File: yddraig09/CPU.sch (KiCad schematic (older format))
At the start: 6 parts

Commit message: Added RAM/ROM Banking idea
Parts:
- removed U?: SST39SF020, symbol Memory_Flash:SST39SF020
- removed U?: AT28C64B, symbol Ddraig:AT28C64B
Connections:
- net labels removed: A0, A1, A10, A11, A12, A13, A2, A3, A4, A5, A6, A7, A8, A9, RB0, RB1, RB2, RB3
- wire segments 124 -> 67
- no-connect marks 1 -> 0

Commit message: Some tidying up of 6809 project
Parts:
- added C? (x2): 10uF, Capacitor_THT:CP_Radial_D5.0mm_P2.50mm, symbol Device:CP
- added C?: 10nF, Capacitor_THT:C_Disc_D3.8mm_W2.6mm_P2.50mm, symbol Device:C
- added C? (x2): 22pF, Capacitor_THT:C_Disc_D5.0mm_W2.5mm_P2.50mm, symbol Device:C
- added C?: 5pF, Capacitor_THT:C_Disc_D5.0mm_W2.5mm_P2.50mm, symbol Device:C
- added J?: ExtReset, Connector_PinHeader_2.54mm:PinHeader_1x02_P2.54mm_Vertical, symbol Connector_Generic:Conn_01x02
- added R?: 10K, Resistor_THT:R_Axial_DIN0207_L6.3mm_D2.5mm_P10.16mm_Horizontal, symbol Device:R
- added R?: 38K, Resistor_THT:R_Axial_DIN0207_L6.3mm_D2.5mm_P10.16mm_Horizontal, symbol Device:R
- added R? (x4): 4k7, symbol Device:R
- added R?: 4M7, Resistor_THT:R_Axial_DIN0207_L6.3mm_D2.5mm_P10.16mm_Horizontal, symbol Device:R
- added R?: 2K2, Resistor_THT:R_Axial_DIN0207_L6.3mm_D2.5mm_P10.16mm_Horizontal, symbol Device:R
- added SW?: Reset, Button_Switch_THT:SW_PUSH_6mm_H4.3mm, symbol Switch:SW_SPST
- added U?: NE555P, Package_DIP:DIP-8_W7.62mm, symbol Timer:NE555P
- added U? (x7): 74HCT04, symbol 74xx:74HCT04
- added Y?: 8Mhz, Crystal:Crystal_HC50_Vertical, symbol Device:Crystal
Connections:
- net +5V: now also U?.39 (TSC), R?.1, R?.1, R?.1, R?.1, R?.1, R?.1, U?.14 (VCC), U?.4 (R), U?.8 (VCC)
- net GND: now also C?.2, C?.2, C?.2, C?.2, C?.2, C?.2, J?.2 (Pin_2), SW?.1 (A), U?.1 (GND), U?.11, U?.5, U?.7 (GND), U?.9
- net RD~WR: now also U?.32 (R/~W)
- net CPU_A2: now reaches U?.10 (A2)
- net CPU_A3: now reaches U?.11 (A3)
- net CPU_A4: now reaches U?.12 (A4)
- net CPU_A5: now reaches U?.13 (A5)
- net CPU_A6: now reaches U?.14 (A6)
- net CPU_A7: now reaches U?.15 (A7)
- net CPU_A8: now reaches U?.16 (A8)
- net CPU_A9: now reaches U?.17 (A9)
- net CPU_A10: now reaches U?.18 (A10)
- net CPU_A11: now reaches U?.19 (A11)
- net at U?.2 (~NMI): now also R?.2
- net CPU_A12: now reaches U?.20 (A12)
- net CPU_A13: now reaches U?.21 (A13)
- net CPU_A14: now reaches U?.22 (A14)
- net CPU_A15: now reaches U?.23 (A15)
- net at U?.3 (~IRQ): now also R?.2
- net ~RESET: now reaches U?.37 (~RESET)
- net ~RESET: now also U?.12
- net at U?.4 (~FIRQ): now also R?.2
- net ~HALT: now reaches U?.40 (~HALT)
- net ~HALT: now also R?.2
- net BS: now reaches U?.5 (BS)
- net BA: now reaches U?.6 (BA)
- net CPU_A0: now reaches U?.8 (A0)
- net CPU_A1: now reaches U?.9 (A1)
- net CLK8M renamed CLK_8MHZ
- net CLK_8MHZ: now also C?.1, R?.1
- net D0 renamed CPU_D0
- net D1 renamed CPU_D1
- net D2 renamed CPU_D2
- net D3 renamed CPU_D3
- net D4 renamed CPU_D4
- net D5 renamed CPU_D5
- net D6 renamed CPU_D6
- net D7 renamed CPU_D7
- new net: C?.1, J?.1 (Pin_1), R?.2, SW?.2 (B), U?.2 (TR)
- new net: C?.1, U?.5 (CV)
- new net: C?.1, R?.2, U?.6 (THR), U?.7 (DIS)
- new net: C?.1, R?.1, U?.1, Y?.2
- new net: C?.1, R?.2, U?.2, U?.3, Y?.1
- new net: R?.2, U?.4
- new net RESET: U?.13, U?.3 (Q)
- no-connect marks 0 -> 6
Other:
- moved on the sheet: U?, U?A, U?B, U?C

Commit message: more progress
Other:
- moved on the sheet: C?, R?, U?A, U?B, Y?

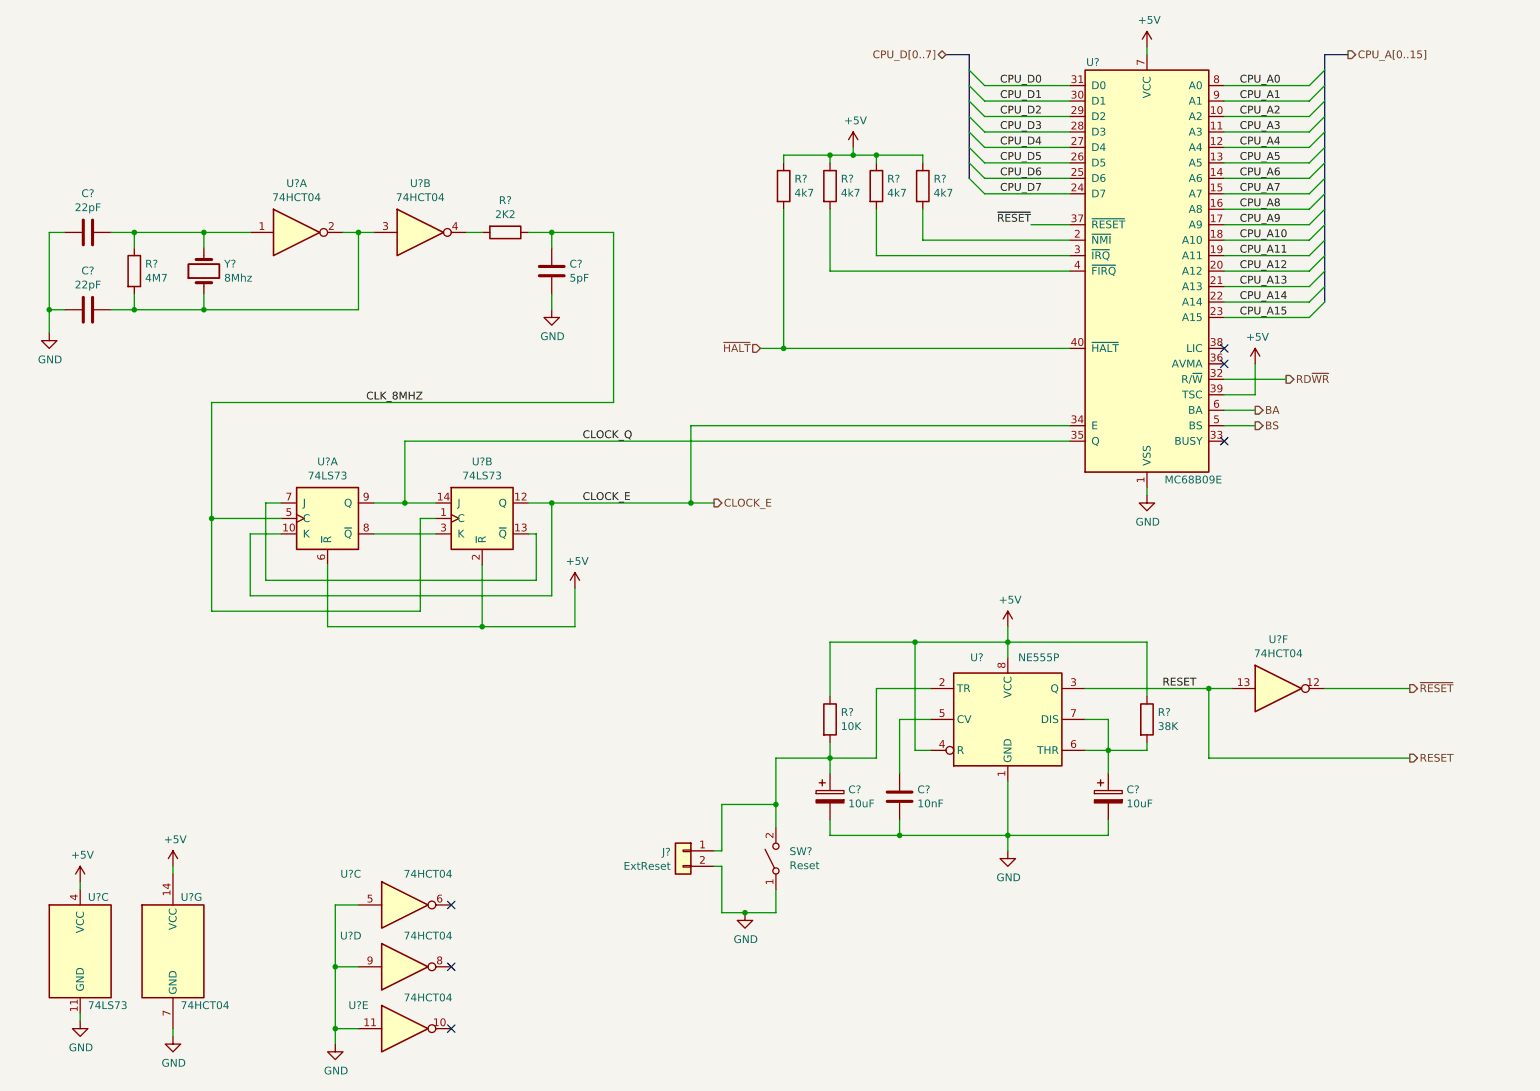
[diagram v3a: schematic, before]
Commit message: ddraig09: Added decode logic and expansion slot
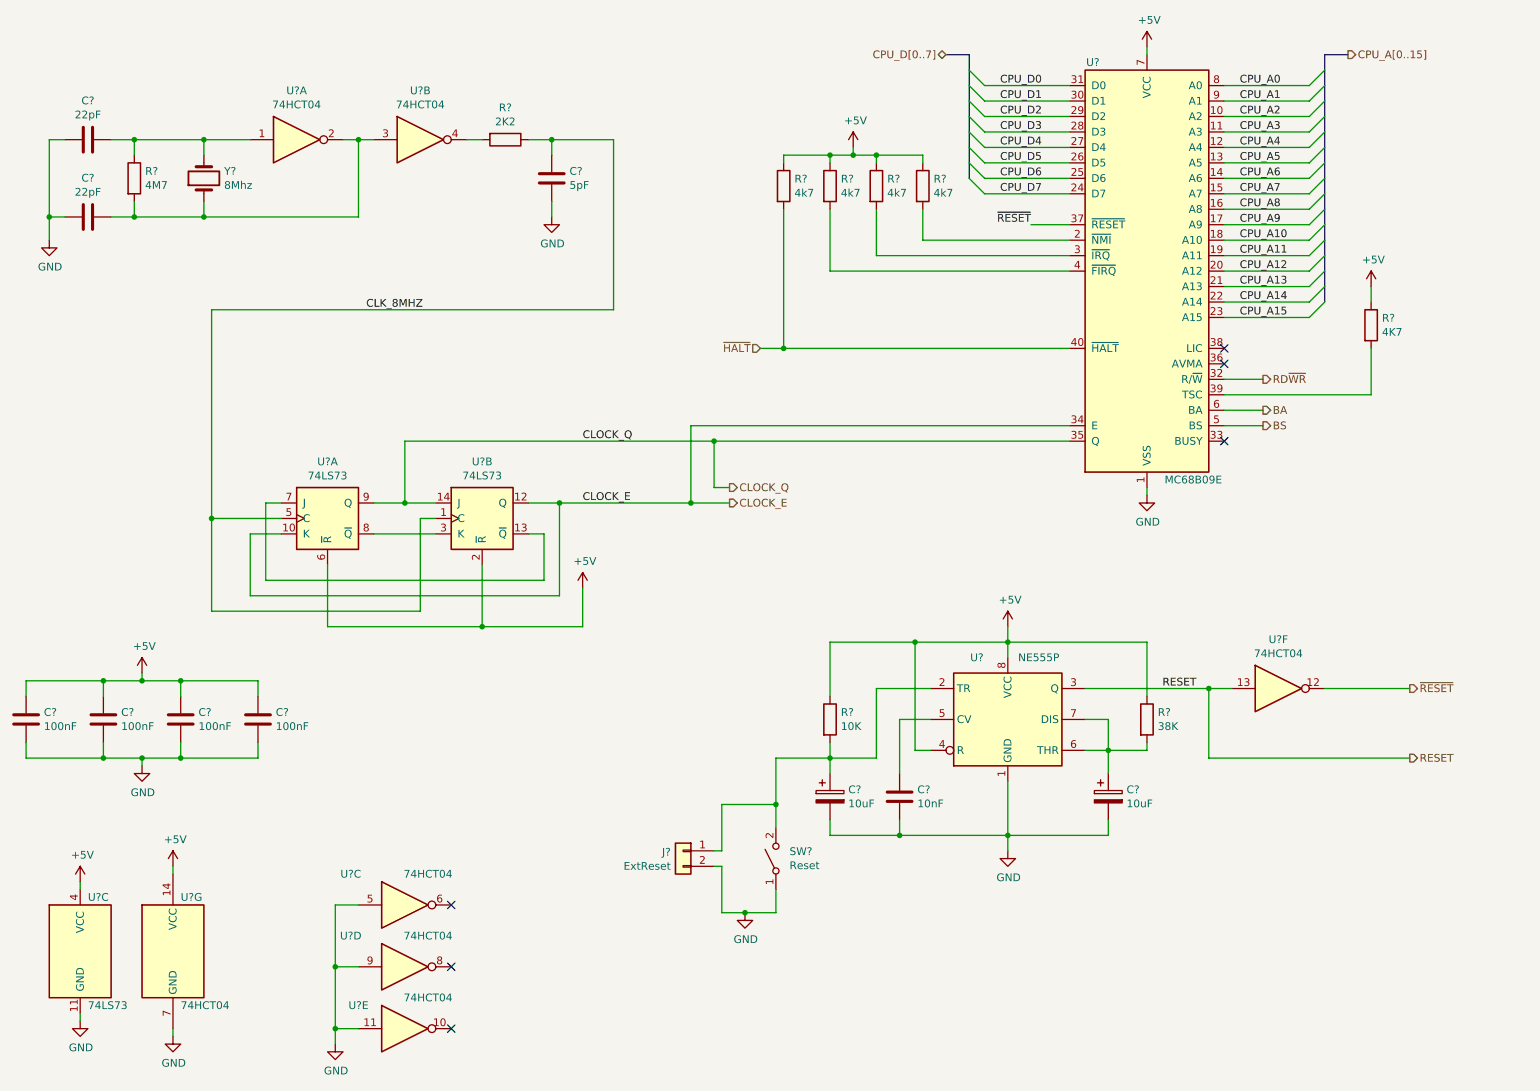
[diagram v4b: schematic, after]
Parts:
- added C? (x4): 100nF, symbol Device:C
- added R?: 4K7, symbol Device:R
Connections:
- net +5V: now also C?.1, C?.1, C?.1, C?.1, R?.1; no longer U?.39 (TSC)
- net GND: now also C?.2, C?.2, C?.2, C?.2
- new net: R?.2, U?.39 (TSC)
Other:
- moved on the sheet: C?, R?, U?A, U?B, Y?

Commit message: ddraig09: initial design done
Need to be reviewed and decode on additional uses for IO but passed DRC
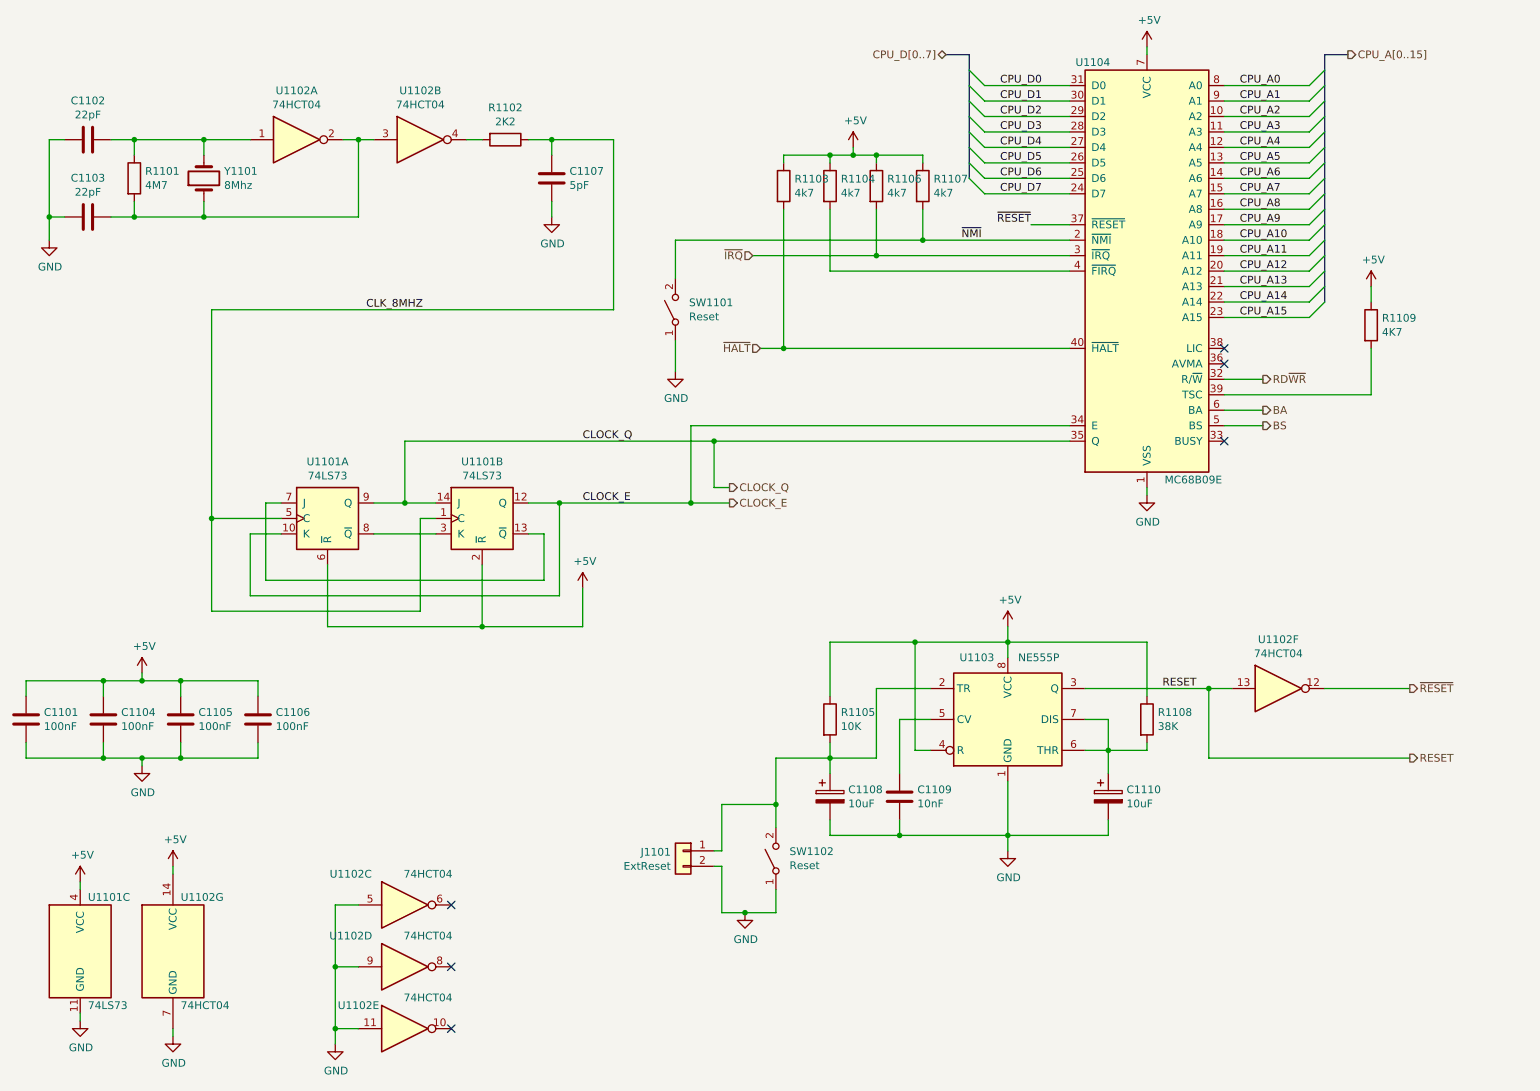
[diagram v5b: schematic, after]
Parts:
- added SW1101: Reset, Button_Switch_THT:SW_PUSH_6mm_H4.3mm, symbol Switch:SW_SPST
- gave numbers to parts that had none: 26
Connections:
- net GND: now also SW1101.1 (A)
- net ~NMI: now reaches R1107.2, U1104.2 (~NMI)
- net ~NMI: now also SW1101.2 (B)
- net ~IRQ: now reaches R1106.2, U1104.3 (~IRQ)

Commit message: Asssigned part footprints to most of schematic
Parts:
- C1101, C1104, C1105, C1106: footprint (none) -> Capacitor_THT:C_Disc_D5.0mm_W2.5mm_P2.50mm
- R1103, R1104, R1106, R1107, R1109: footprint (none) -> Resistor_THT:R_Axial_DIN0207_L6.3mm_D2.5mm_P10.16mm_Horizontal
- U1101, U1102: footprint (none) -> Package_DIP:DIP-14_W7.62mm_Socket
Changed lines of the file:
@@
 F 0 "U1101" H 1750 7200 50  0000 L CNN
 F 1 "74LS73" H 1750 6500 50  0000 L CNN
-F 2 "" H 1700 6850 50  0001 C CNN
+F 2 "Package_DIP:DIP-14_W7.62mm_Socket" H 1700 6850 50  0001 C CNN
 F 3 "http://www.ti.com/lit/gpn/sn74LS73" H 1700 6850 50  0001 C CNN
 	3    1700 6850
@@
 F 0 "R1106" H 6920 1946 50  0000 L CNN
 F 1 "4k7" H 6920 1855 50  0000 L CNN
-F 2 "" V 6780 1900 50  0001 C CNN
+F 2 "Resistor_THT:R_Axial_DIN0207_L6.3mm_D2.5mm_P10.16mm_Horizontal" V 6780 1900 50  0001 C CNN
 F 3 "~" H 6850 1900 50  0001 C CNN
 	1    6850 1900
@@
 F 0 "R1107" H 7220 1946 50  0000 L CNN
 F 1 "4k7" H 7220 1855 50  0000 L CNN
-F 2 "" V 7080 1900 50  0001 C CNN
+F 2 "Resistor_THT:R_Axial_DIN0207_L6.3mm_D2.5mm_P10.16mm_Horizontal" V 7080 1900 50  0001 C CNN
 F 3 "~" H 7150 1900 50  0001 C CNN
 	1    7150 1900
@@
 F 0 "R1103" H 6320 1946 50  0000 L CNN
 F 1 "4k7" H 6320 1855 50  0000 L CNN
-F 2 "" V 6180 1900 50  0001 C CNN
+F 2 "Resistor_THT:R_Axial_DIN0207_L6.3mm_D2.5mm_P10.16mm_Horizontal" V 6180 1900 50  0001 C CNN
 F 3 "~" H 6250 1900 50  0001 C CNN
 	1    6250 1900
@@
 F 0 "R1104" H 6620 1946 50  0000 L CNN
 F 1 "4k7" H 6620 1855 50  0000 L CNN
-F 2 "" V 6480 1900 50  0001 C CNN
+F 2 "Resistor_THT:R_Axial_DIN0207_L6.3mm_D2.5mm_P10.16mm_Horizontal" V 6480 1900 50  0001 C CNN
 F 3 "~" H 6550 1900 50  0001 C CNN
 	1    6550 1900
@@
 F 0 "U1102" H 3450 6750 50  0000 C CNN
 F 1 "74HCT04" H 3950 6750 50  0000 C CNN
-F 2 "" H 3800 6550 50  0001 C CNN
+F 2 "Package_DIP:DIP-14_W7.62mm_Socket" H 3800 6550 50  0001 C CNN
 F 3 "https://assets.nexperia.com/documents/data-sheet/74HC_HCT04.pdf" H 3800 6550 50  0001 C CNN
 	3    3800 6550
@@
 F 0 "U1102" H 3450 7150 50  0000 C CNN
 F 1 "74HCT04" H 3950 7150 50  0000 C CNN
-F 2 "" H 3800 6950 50  0001 C CNN
+F 2 "Package_DIP:DIP-14_W7.62mm_Socket" H 3800 6950 50  0001 C CNN
 F 3 "https://assets.nexperia.com/documents/data-sheet/74HC_HCT04.pdf" H 3800 6950 50  0001 C CNN
 	4    3800 6950
@@
 F 0 "U1102" H 3500 7500 50  0000 C CNN
 F 1 "74HCT04" H 3950 7550 50  0000 C CNN
-F 2 "" H 3800 7350 50  0001 C CNN
+F 2 "Package_DIP:DIP-14_W7.62mm_Socket" H 3800 7350 50  0001 C CNN
 F 3 "https://assets.nexperia.com/documents/data-sheet/74HC_HCT04.pdf" H 3800 7350 50  0001 C CNN
 	5    3800 7350
@@
 F 0 "U1102" H 9450 5467 50  0000 C CNN
 F 1 "74HCT04" H 9450 5376 50  0000 C CNN
-F 2 "" H 9450 5150 50  0001 C CNN
+F 2 "Package_DIP:DIP-14_W7.62mm_Socket" H 9450 5150 50  0001 C CNN
 F 3 "https://assets.nexperia.com/documents/data-sheet/74HC_HCT04.pdf" H 9450 5150 50  0001 C CNN
 	6    9450 5150
@@
 F 0 "U1102" H 2350 7200 50  0000 L CNN
 F 1 "74HCT04" H 2350 6500 50  0000 L CNN
-F 2 "" H 2300 6850 50  0001 C CNN
+F 2 "Package_DIP:DIP-14_W7.62mm_Socket" H 2300 6850 50  0001 C CNN
 F 3 "https://assets.nexperia.com/documents/data-sheet/74HC_HCT04.pdf" H 2300 6850 50  0001 C CNN
 	7    2300 6850
@@
 F 0 "U1102" H 3900 1917 50  0000 C CNN
 F 1 "74HCT04" H 3900 1826 50  0000 C CNN
-F 2 "" H 3900 1600 50  0001 C CNN
+F 2 "Package_DIP:DIP-14_W7.62mm_Socket" H 3900 1600 50  0001 C CNN
 F 3 "https://assets.nexperia.com/documents/data-sheet/74HC_HCT04.pdf" H 3900 1600 50  0001 C CNN
 	2    3900 1600
@@
 F 0 "U1102" H 3100 1917 50  0000 C CNN
 F 1 "74HCT04" H 3100 1826 50  0000 C CNN
-F 2 "" H 3100 1600 50  0001 C CNN
+F 2 "Package_DIP:DIP-14_W7.62mm_Socket" H 3100 1600 50  0001 C CNN
 F 3 "https://assets.nexperia.com/documents/data-sheet/74HC_HCT04.pdf" H 3100 1600 50  0001 C CNN
 	1    3100 1600
@@
 F 0 "U1101" H 3300 4417 50  0000 C CNN
 F 1 "74LS73" H 3300 4326 50  0000 C CNN
-F 2 "" H 3300 4050 50  0001 C CNN
+F 2 "Package_DIP:DIP-14_W7.62mm_Socket" H 3300 4050 50  0001 C CNN
 F 3 "http://www.ti.com/lit/gpn/sn74LS73" H 3300 4050 50  0001 C CNN
 	1    3300 4050
@@
 F 0 "U1101" H 4300 4417 50  0000 C CNN
 F 1 "74LS73" H 4300 4326 50  0000 C CNN
-F 2 "" H 4300 4050 50  0001 C CNN
+F 2 "Package_DIP:DIP-14_W7.62mm_Socket" H 4300 4050 50  0001 C CNN
 F 3 "http://www.ti.com/lit/gpn/sn74LS73" H 4300 4050 50  0001 C CNN
 	2    4300 4050
@@
 F 0 "R1109" H 10120 2846 50  0000 L CNN
 F 1 "4K7" H 10120 2755 50  0000 L CNN
-F 2 "" V 9980 2800 50  0001 C CNN
+F 2 "Resistor_THT:R_Axial_DIN0207_L6.3mm_D2.5mm_P10.16mm_Horizontal" V 9980 2800 50  0001 C CNN
 F 3 "~" H 10050 2800 50  0001 C CNN
 	1    10050 2800
@@
 F 0 "C1101" H 1465 5396 50  0000 L CNN
 F 1 "100nF" H 1465 5305 50  0000 L CNN
-F 2 "" H 1388 5200 50  0001 C CNN
+F 2 "Capacitor_THT:C_Disc_D5.0mm_W2.5mm_P2.50mm" H 1388 5200 50  0001 C CNN
 F 3 "~" H 1350 5350 50  0001 C CNN
 	1    1350 5350
@@
 F 0 "C1104" H 1965 5396 50  0000 L CNN
 F 1 "100nF" H 1965 5305 50  0000 L CNN
-F 2 "" H 1888 5200 50  0001 C CNN
+F 2 "Capacitor_THT:C_Disc_D5.0mm_W2.5mm_P2.50mm" H 1888 5200 50  0001 C CNN
 F 3 "~" H 1850 5350 50  0001 C CNN
 	1    1850 5350
@@
 F 0 "C1105" H 2465 5396 50  0000 L CNN
 F 1 "100nF" H 2465 5305 50  0000 L CNN
-F 2 "" H 2388 5200 50  0001 C CNN
+F 2 "Capacitor_THT:C_Disc_D5.0mm_W2.5mm_P2.50mm" H 2388 5200 50  0001 C CNN
 F 3 "~" H 2350 5350 50  0001 C CNN
 	1    2350 5350
@@
 F 0 "C1106" H 2965 5396 50  0000 L CNN
 F 1 "100nF" H 2965 5305 50  0000 L CNN
-F 2 "" H 2888 5200 50  0001 C CNN
+F 2 "Capacitor_THT:C_Disc_D5.0mm_W2.5mm_P2.50mm" H 2888 5200 50  0001 C CNN
 F 3 "~" H 2850 5350 50  0001 C CNN
 	1    2850 5350

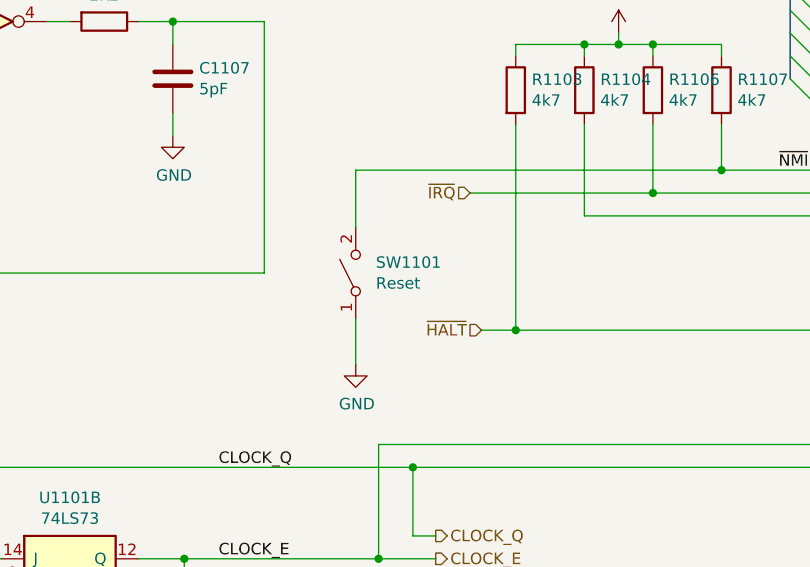
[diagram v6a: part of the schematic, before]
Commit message: Started working on 6809 board layout
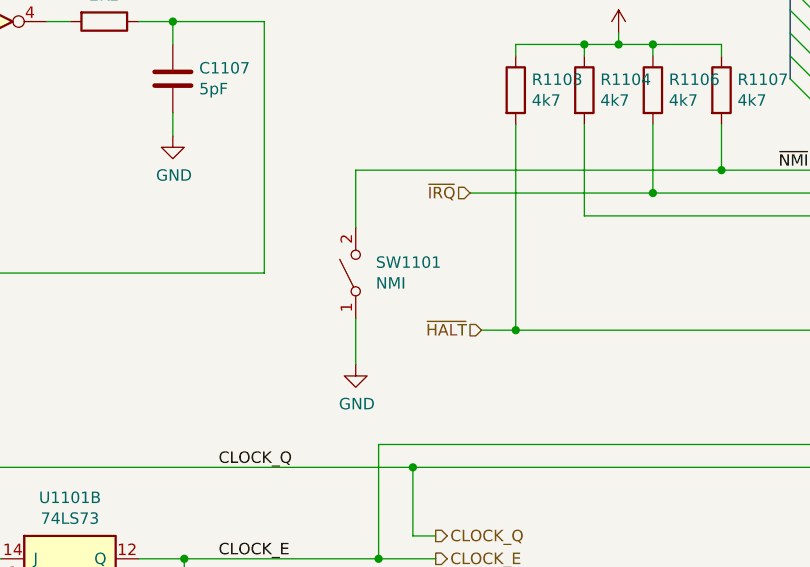
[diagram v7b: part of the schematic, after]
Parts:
- SW1101: value Reset -> NMI
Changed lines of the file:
@@
 AR Path="/60AC674F/616288D9" Ref="SW1101"  Part="1"
 F 0 "SW1101" V 5596 2612 50  0000 R CNN
-F 1 "Reset" V 5505 2612 50  0000 R CNN
+F 1 "NMI" V 5505 2612 50  0000 R CNN
 F 2 "Button_Switch_THT:SW_PUSH_6mm_H4.3mm" H 5550 2700 50  0001 C CNN
 F 3 "~" H 5550 2700 50  0001 C CNN

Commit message: Added initial 6809 board layout design
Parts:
- U1104: footprint Package_DIP:DIP-40_W15.24mm -> Package_DIP:DIP-40_W15.24mm_Socket
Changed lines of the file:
@@
 F 0 "U1104" H 8250 3800 50  0000 C CNN
 F 1 "MC68B09E" H 8900 1100 50  0000 C CNN
-F 2 "Package_DIP:DIP-40_W15.24mm" H 8600 950 50  0001 C CNN
+F 2 "Package_DIP:DIP-40_W15.24mm_Socket" H 8600 950 50  0001 C CNN
 F 3 "http://pdf.datasheetcatalog.com/datasheet/motorola/MC68B09S.pdf" H 8500 3875 50  0001 C CNN
 	1    8600 2450
